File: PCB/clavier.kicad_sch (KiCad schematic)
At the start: 4 parts

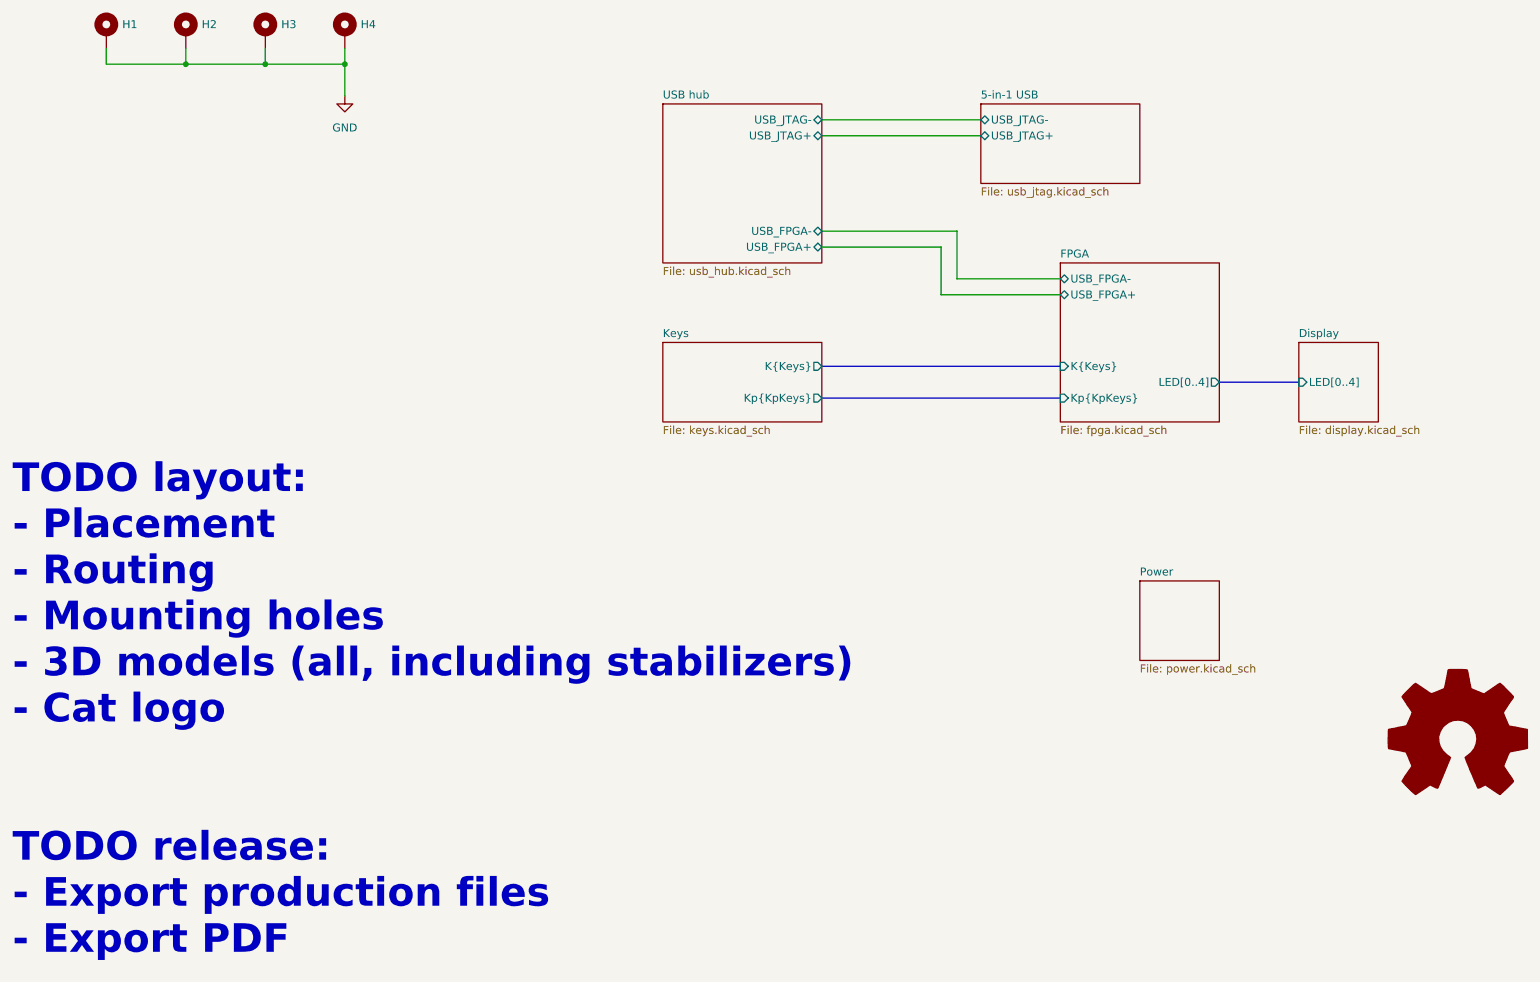
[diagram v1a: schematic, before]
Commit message: Place and route peripheral components
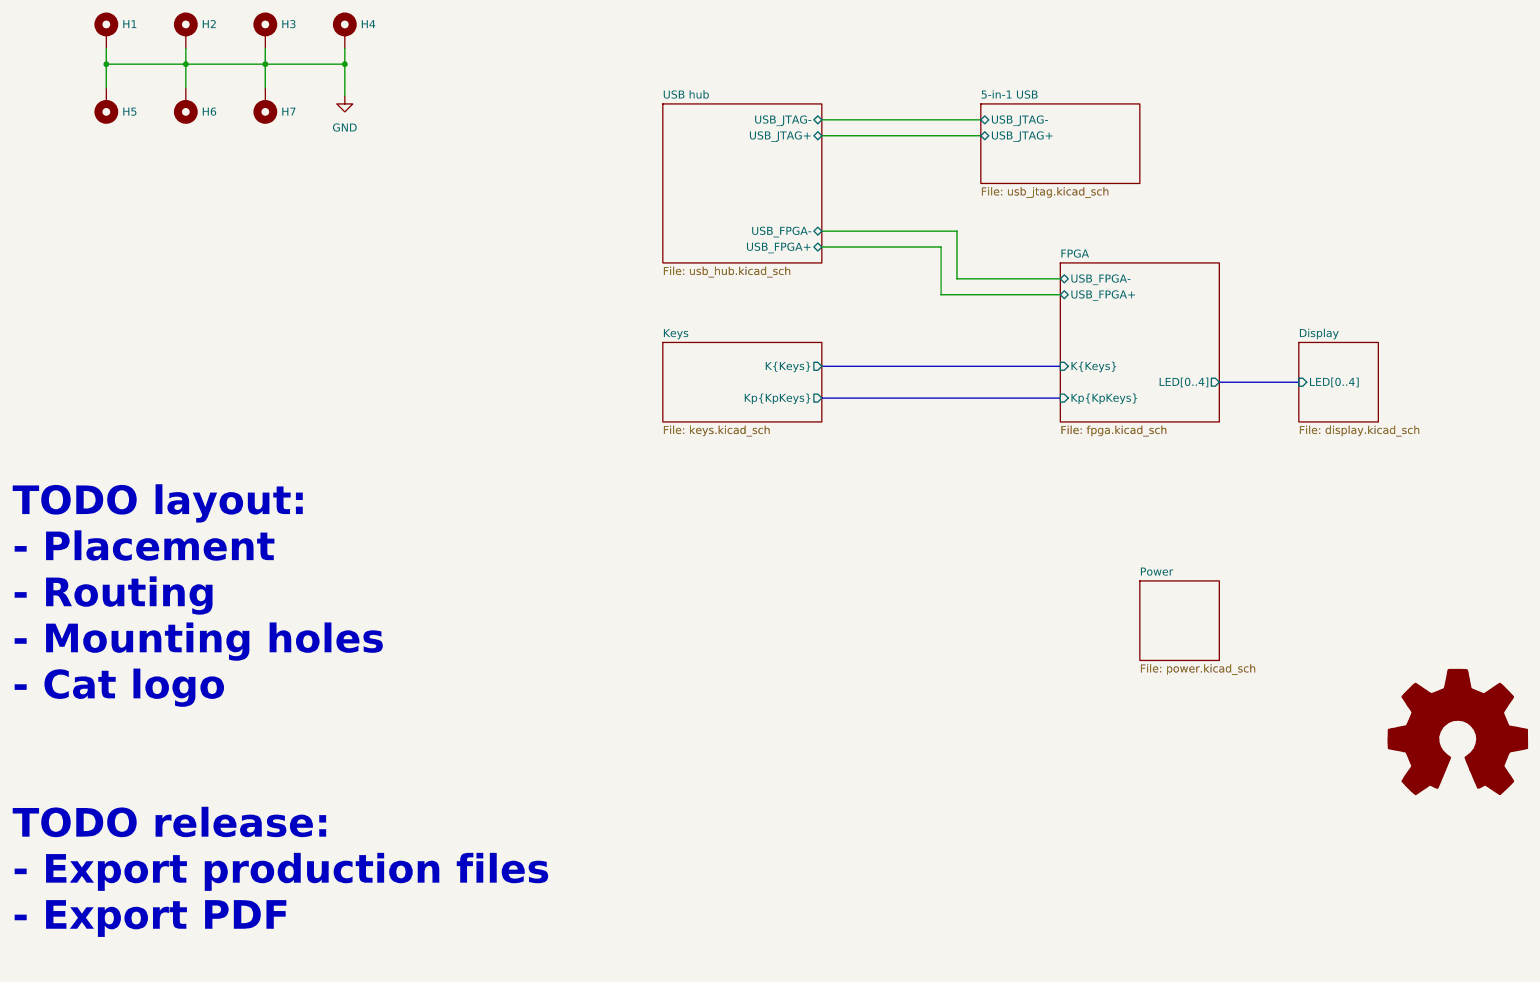
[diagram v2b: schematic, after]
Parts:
- added H2, H3, H6: MountingHole_Pad, MountingHole:MountingHole_3.2mm_M3_ISO7380_Pad_TopBottom, symbol Mechanical:MountingHole_Pad
- renumbered H2 to H4, H3 to H5, H4 to H7
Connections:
- net GND: now also H2.1, H3.1, H6.1
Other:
- note added: "TODO layout: - Placement - Routing - Mounting holes - Cat logo TODO release: - Export production files - Export PDF"
- note removed: "TODO layout: - Placement - Routing - Mounting holes - 3D models (all, including stabilizers) - Cat logo TODO release: - Export production files - Export PDF"
- moved on the sheet: H4, H5, H7
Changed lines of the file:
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@@
 		(comment 1 "SPDX-License-Identifier: CERN-OHL-P-2.0")
 	)
-	(text "TODO layout:\n- Placement\n- Routing\n- Mounting holes\n- 3D models (all, including stabilizers)\n- Cat logo\n\n\nTODO release:\n- Export production files\n- Export PDF"
+	(text "TODO layout:\n- Placement\n- Routing\n- Mounting holes\n- Cat logo\n\n\nTODO release:\n- Export production files\n- Export PDF"
 		(exclude_from_sim no)
 		(at 23.114 147.574 0)
@@
 	)
 	(junction
+		(at 38.1 44.45)
+		(diameter 0)
+		(color 0 0 0 0)
+	)
+	(junction
 		(at 63.5 44.45)
 		(diameter 0)
@@
 	(wire
 		(pts
+			(xy 38.1 44.45) (xy 38.1 48.26)
+		)
+		(stroke
+			(width 0)
+			(type default)
+		)
+	)
+	(wire
+		(pts
 			(xy 152.4 73.66) (xy 171.45 73.66)
 		)
@@
 	(wire
 		(pts
+			(xy 63.5 44.45) (xy 63.5 48.26)
+		)
+		(stroke
+			(width 0)
+			(type default)
+		)
+	)
+	(wire
+		(pts
 			(xy 152.4 71.12) (xy 173.99 71.12)
 		)
@@
 		(pts
 			(xy 152.4 97.79) (xy 190.5 97.79)
+		)
+		(stroke
+			(width 0)
+			(type default)
+		)
+	)
+	(wire
+		(pts
+			(xy 50.8 44.45) (xy 50.8 48.26)
 		)
 		(stroke
@@
 	(symbol
 		(lib_id "Mechanical:MountingHole_Pad")
-		(at 63.5 39.37 0)
+		(at 38.1 50.8 180)
 		(unit 1)
 		(exclude_from_sim no)
@@
 		(dnp no)
 		(fields_autoplaced yes)
-		(property "Reference" "H3"
-			(at 66.04 38.0999 0)
-			(effects
-				(font
-					(size 1.27 1.27)
-				)
-				(justify left)
+		(property "Reference" "H5"
+			(at 40.64 52.0699 0)
+			(effects
+				(font
+					(size 1.27 1.27)
+				)
+				(justify right)
 			)
 		)
 		(property "Value" "MountingHole_Pad"
-			(at 66.04 39.3699 0)
+			(at 35.56 50.8001 0)
 			(effects
 				(font
@@
 		)
 		(property "Footprint" "MountingHole:MountingHole_3.2mm_M3_ISO7380_Pad_TopBottom"
-			(at 63.5 39.37 0)
+			(at 38.1 50.8 0)
 			(effects
 				(font
@@
 		)
 		(property "Datasheet" "~"
-			(at 63.5 39.37 0)
+			(at 38.1 50.8 0)
 			(effects
 				(font
@@
 		)
 		(property "Description" "Mounting Hole with connection"
-			(at 63.5 39.37 0)
+			(at 38.1 50.8 0)
 			(effects
 				(font
@@
 			(project "clavier"
 				(path "/6362c6e0-59ef-40d3-b6e0-7e9dfe7b9b20"
-					(reference "H3")
+					(reference "H5")
 					(unit 1)
 				)
@@
 	(symbol
 		(lib_id "Mechanical:MountingHole_Pad")
-		(at 50.8 39.37 0)
-		(unit 1)
-		(exclude_from_sim no)
-		(in_bom no)
-		(on_board yes)
-		(dnp no)
-		(fields_autoplaced yes)
-		(property "Reference" "H2"
-			(at 53.34 38.0999 0)
-			(effects
-				(font
-					(size 1.27 1.27)
-				)
-				(justify left)
-			)
-		)
-		(property "Value" "MountingHole_Pad"
-			(at 53.34 39.3699 0)
-			(effects
-				(font
-					(size 1.27 1.27)
-				)
-				(justify left)
-				(hide yes)
-			)
-		)
-		(property "Footprint" "MountingHole:MountingHole_3.2mm_M3_ISO7380_Pad_TopBottom"
-			(at 50.8 39.37 0)
-			(effects
-				(font
-					(size 1.27 1.27)
-				)
-				(hide yes)
-			)
-		)
-		(property "Datasheet" "~"
-			(at 50.8 39.37 0)
-			(effects
-				(font
-					(size 1.27 1.27)
-				)
-				(hide yes)
-			)
-		)
-		(property "Description" "Mounting Hole with connection"
-			(at 50.8 39.37 0)
-			(effects
-				(font
-					(size 1.27 1.27)
-				)
-				(hide yes)
-			)
-		)
-		(pin "1"
-		)
-		(instances
-			(project "clavier"
-				(path "/6362c6e0-59ef-40d3-b6e0-7e9dfe7b9b20"
-					(reference "H2")
-					(unit 1)
-				)
-			)
-		)
-	)
-	(symbol
-		(lib_id "Mechanical:MountingHole_Pad")
 		(at 76.2 39.37 0)
 		(unit 1)
@@
 				(path "/6362c6e0-59ef-40d3-b6e0-7e9dfe7b9b20"
 					(reference "H4")
+					(unit 1)
+				)
+			)
+		)
+	)
+	(symbol
+		(lib_id "Mechanical:MountingHole_Pad")
+		(at 50.8 50.8 180)
+		(unit 1)
+		(exclude_from_sim no)
+		(in_bom no)
+		(on_board yes)
+		(dnp no)
+		(fields_autoplaced yes)
+		(property "Reference" "H6"
+			(at 53.34 52.0699 0)
+			(effects
+				(font
+					(size 1.27 1.27)
+				)
+				(justify right)
+			)
+		)
+		(property "Value" "MountingHole_Pad"
+			(at 48.26 50.8001 0)
+			(effects
+				(font
+					(size 1.27 1.27)
+				)
+				(justify left)
+				(hide yes)
+			)
+		)
+		(property "Footprint" "MountingHole:MountingHole_3.2mm_M3_ISO7380_Pad_TopBottom"
+			(at 50.8 50.8 0)
+			(effects
+				(font
+					(size 1.27 1.27)
+				)
+				(hide yes)
+			)
+		)
+		(property "Datasheet" "~"
+			(at 50.8 50.8 0)
+			(effects
+				(font
+					(size 1.27 1.27)
+				)
+				(hide yes)
+			)
+		)
+		(property "Description" "Mounting Hole with connection"
+			(at 50.8 50.8 0)
+			(effects
+				(font
+					(size 1.27 1.27)
+				)
+				(hide yes)
+			)
+		)
+		(pin "1"
+		)
+		(instances
+			(project "clavier"
+				(path "/6362c6e0-59ef-40d3-b6e0-7e9dfe7b9b20"
+					(reference "H6")
+					(unit 1)
+				)
+			)
+		)
+	)
+	(symbol
+		(lib_id "Mechanical:MountingHole_Pad")
+		(at 63.5 39.37 0)
+		(unit 1)
+		(exclude_from_sim no)
+		(in_bom no)
+		(on_board yes)
+		(dnp no)
+		(fields_autoplaced yes)
+		(property "Reference" "H3"
+			(at 66.04 38.0999 0)
+			(effects
+				(font
+					(size 1.27 1.27)
+				)
+				(justify left)
+			)
+		)
+		(property "Value" "MountingHole_Pad"
+			(at 66.04 39.3699 0)
+			(effects
+				(font
+					(size 1.27 1.27)
+				)
+				(justify left)
+				(hide yes)
+			)
+		)
+		(property "Footprint" "MountingHole:MountingHole_3.2mm_M3_ISO7380_Pad_TopBottom"
+			(at 63.5 39.37 0)
+			(effects
+				(font
+					(size 1.27 1.27)
+				)
+				(hide yes)
+			)
+		)
+		(property "Datasheet" "~"
+			(at 63.5 39.37 0)
+			(effects
+				(font
+					(size 1.27 1.27)
+				)
+				(hide yes)
+			)
+		)
+		(property "Description" "Mounting Hole with connection"
+			(at 63.5 39.37 0)
+			(effects
+				(font
+					(size 1.27 1.27)
+				)
+				(hide yes)
+			)
+		)
+		(pin "1"
+		)
+		(instances
+			(project "clavier"
+				(path "/6362c6e0-59ef-40d3-b6e0-7e9dfe7b9b20"
+					(reference "H3")
+					(unit 1)
+				)
+			)
+		)
+	)
+	(symbol
+		(lib_id "Mechanical:MountingHole_Pad")
+		(at 63.5 50.8 180)
+		(unit 1)
+		(exclude_from_sim no)
+		(in_bom no)
+		(on_board yes)
+		(dnp no)
+		(fields_autoplaced yes)
+		(property "Reference" "H7"
+			(at 66.04 52.0699 0)
+			(effects
+				(font
+					(size 1.27 1.27)
+				)
+				(justify right)
+			)
+		)
+		(property "Value" "MountingHole_Pad"
+			(at 60.96 50.8001 0)
+			(effects
+				(font
+					(size 1.27 1.27)
+				)
+				(justify left)
+				(hide yes)
+			)
+		)
+		(property "Footprint" "MountingHole:MountingHole_3.2mm_M3_ISO7380_Pad_TopBottom"
+			(at 63.5 50.8 0)
+			(effects
+				(font
+					(size 1.27 1.27)
+				)
+				(hide yes)
+			)
+		)
+		(property "Datasheet" "~"
+			(at 63.5 50.8 0)
+			(effects
+				(font
+					(size 1.27 1.27)
+				)
+				(hide yes)
+			)
+		)
+		(property "Description" "Mounting Hole with connection"
+			(at 63.5 50.8 0)
+			(effects
+				(font
+					(size 1.27 1.27)
+				)
+				(hide yes)
+			)
+		)
+		(pin "1"
+		)
+		(instances
+			(project "clavier"
+				(path "/6362c6e0-59ef-40d3-b6e0-7e9dfe7b9b20"
+					(reference "H7")
 					(unit 1)
 				)
@@
 					(unit 1)
 				)
+			)
+		)
+	)
+	(symbol
+		(lib_id "Mechanical:MountingHole_Pad")
+		(at 50.8 39.37 0)
+		(unit 1)
+		(exclude_from_sim no)
+		(in_bom no)
+		(on_board yes)
+		(dnp no)
+		(fields_autoplaced yes)
+		(property "Reference" "H2"
+			(at 53.34 38.0999 0)
+			(effects
+				(font
+					(size 1.27 1.27)
+				)
+				(justify left)
+			)
+		)
+		(property "Value" "MountingHole_Pad"
+			(at 53.34 39.3699 0)
+			(effects
+				(font
+					(size 1.27 1.27)
+				)
+				(justify left)
+				(hide yes)
+			)
+		)
+		(property "Footprint" "MountingHole:MountingHole_3.2mm_M3_ISO7380_Pad_TopBottom"
+			(at 50.8 39.37 0)
+			(effects
+				(font
+					(size 1.27 1.27)
+				)
+				(hide yes)
+			)
+		)
+		(property "Datasheet" "~"
+			(at 50.8 39.37 0)
+			(effects
+				(font
+					(size 1.27 1.27)
+				)
+				(hide yes)
+			)
+		)
+		(property "Description" "Mounting Hole with connection"
+			(at 50.8 39.37 0)
+			(effects
+				(font
+					(size 1.27 1.27)
+				)
+				(hide yes)
+			)
+		)
+		(pin "1"
+		)
+		(instances
+			(project "clavier"
+				(path "/6362c6e0-59ef-40d3-b6e0-7e9dfe7b9b20"
+					(reference "H2")
+					(unit 1)
+				)

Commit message: Route all critical signals
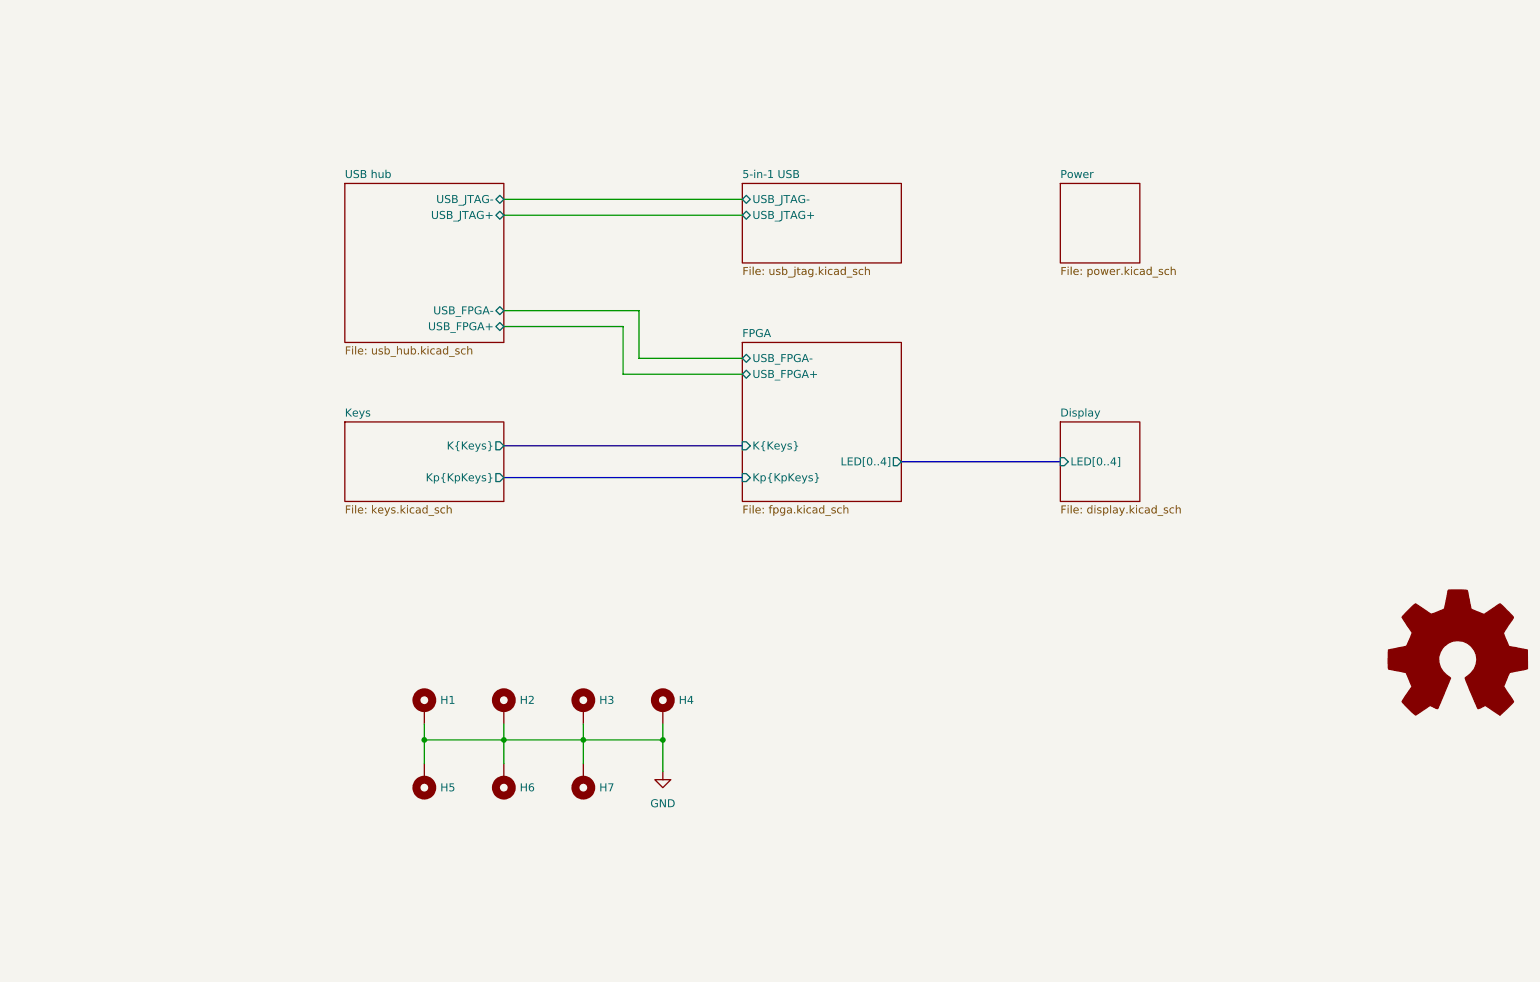
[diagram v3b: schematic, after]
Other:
- note removed: "TODO layout: - Placement - Routing - Mounting holes - Cat logo TODO release: - Export production files - Export PDF"
- moved on the sheet: H1, H2, H3, H4, H5, H6, H7

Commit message: Complete the PCB routing
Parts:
- added OSHW1: Logo_Open_Hardware_Large, Symbol:OSHW-Symbol_13.4x12mm_SilkScreen, symbol Graphic:Logo_Open_Hardware_Large
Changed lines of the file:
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@@
 	(title_block
 		(title "Clavier - Overview")
-		(date "2025-06-21")
+		(date "2025-06-22")
 		(rev "1.0")
 		(company "Copyright (c) 2025 L. Sartory")
@@
 		(exclude_from_sim yes)
 		(in_bom no)
-		(on_board no)
+		(on_board yes)
 		(dnp no)
 		(fields_autoplaced yes)
-		(property "Reference" "#SYM1"
+		(property "Reference" "OSHW1"
 			(at 254 127 0)
 			(effects
@@
 			)
 		)
-		(property "Footprint" ""
+		(property "Footprint" "Symbol:OSHW-Symbol_13.4x12mm_SilkScreen"
 			(at 254 139.7 0)
 			(effects
@@
 			(project ""
 				(path "/6362c6e0-59ef-40d3-b6e0-7e9dfe7b9b20"
-					(reference "#SYM1")
+					(reference "OSHW1")
 					(unit 1)
 				)
